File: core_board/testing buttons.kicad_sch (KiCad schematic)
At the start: 0 parts

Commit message: Import Button Schematic
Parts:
- added D10, D6, D7, D8, D9: Blue, symbol Device:LED
- added D2, D3, D4, D5: Orange, symbol Device:LED
- added Q2, Q3, Q4, Q5, Q6: PMOS, symbol Simulation_SPICE:PMOS
- added R10, R7, R8, R9: 2.2k, symbol Device:R_US
- added R11, R12, R13, R14, R15: 1.3k, symbol Device:R_US
- added SW1, SW2, SW3, SW4: SW_Push, symbol Switch:SW_Push
- added SW5: SW_Rotary_1x4_MP, symbol Switch:SW_Rotary_1x4_MP
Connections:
- new net: D9.1 (K), R15.1
- new net: D8.2 (A), Q5.3 (S)
- new net: D5.1 (K), R9.2
- new net: D2.1 (K), R7.2
- new net: D8.1 (K), R14.1
- new net: D10.1 (K), R13.1
- new net: D7.2 (A), Q3.3 (S)
- new net: D4.1 (K), R10.2
- new net: D3.1 (K), R8.2
- new net: D10.2 (A), Q4.3 (S)
- new net: D7.1 (K), R12.1
- new net: D9.2 (A), Q6.3 (S)
- new net: D6.1 (K), R11.1
- new net: D6.2 (A), Q2.3 (S)
- new net +3.3V: Q2.1 (D), Q3.1 (D), Q4.1 (D), Q5.1 (D), Q6.1 (D)
- new net +3V3: D2.2 (A), D3.2 (A), D4.2 (A), D5.2 (A)
- new net Down: R10.1, SW4.2
- new net GND: R11.2, R12.2, R13.2, R14.2, R15.2, SW1.1, SW2.1, SW3.1, SW4.1
- new net Left: R7.1, SW1.2
- new net Right: R9.1, SW3.2
- new net Up: R8.1, SW2.2
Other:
- note added: "Back Cam"
- note added: "GIMBAL"
- note added: "Indicator leds"
- note added: "Mast"
- note added: "PC0"
- note added: "PC2"
- note added: "PC3"
- note added: "PC4"
- note added: "Servo motor"
- note added: "Spare 1"
- note added: "Testing buttons"

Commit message: Finish Schematic
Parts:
- removed SW5: SW_Rotary_1x4_MP, symbol Switch:SW_Rotary_1x4_MP
- added D11, D12: Blue, symbol Device:LED
- added Q7, Q8: PMOS, symbol Simulation_SPICE:PMOS
- added R17, R21: 1.3k, symbol Device:R_US
- added S1: 94HBB08T, CoreBoard:DIPS762W56P254L991H597Q6N, symbol CoreBoard:94HBB08T
- added SW5: SW_SPDT, Package_SO:SOIC-28W_7.5x17.9mm_P1.27mm, symbol Switch:SW_SPDT
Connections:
- net +3.3V is gone; now on net +3V3: Q2.1 (D), Q3.1 (D), Q4.1 (D), Q5.1 (D), Q6.1 (D)
- net +3V3: now also Q7.1 (D), Q8.1 (D), S1.2 (C_1), S1.5 (C_2), SW5.3 (C)
- net GND: now also R17.2, R21.2, SW5.1 (A)
- net TiltRight_LED: now reaches Q5.2 (G)
- net PanLeft_LED: now reaches Q3.2 (G)
- net PanRight_LED: now reaches Q4.2 (G)
- net TiltBack_LED: now reaches Q6.2 (G)
- net PanBack_LED: now reaches Q2.2 (G)
- new net: D11.1 (K), R17.1
- new net: D11.2 (A), Q7.3 (S)
- new net: D12.1 (K), R21.1
- new net: D12.2 (A), Q8.3 (S)
- new net Direction_Switch: SW5.2 (B)
- new net RTRY1: S1.1
- new net RTRY2: S1.4 (2)
- new net RTRY4: S1.3 (4)
- new net SMOCO_LED: Q8.2 (G)
- new net TiltLeft_LED: Q7.2 (G)
- no-connect marks 0 -> 1
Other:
- note removed: "Back Cam"
- note removed: "GIMBAL"
- note removed: "Mast"
- note removed: "PC0"
- note removed: "PC2"
- note removed: "PC3"
- note removed: "PC4"
- note removed: "Servo motor"
- moved on the sheet: D8, D9, Q5, Q6, R14, R15

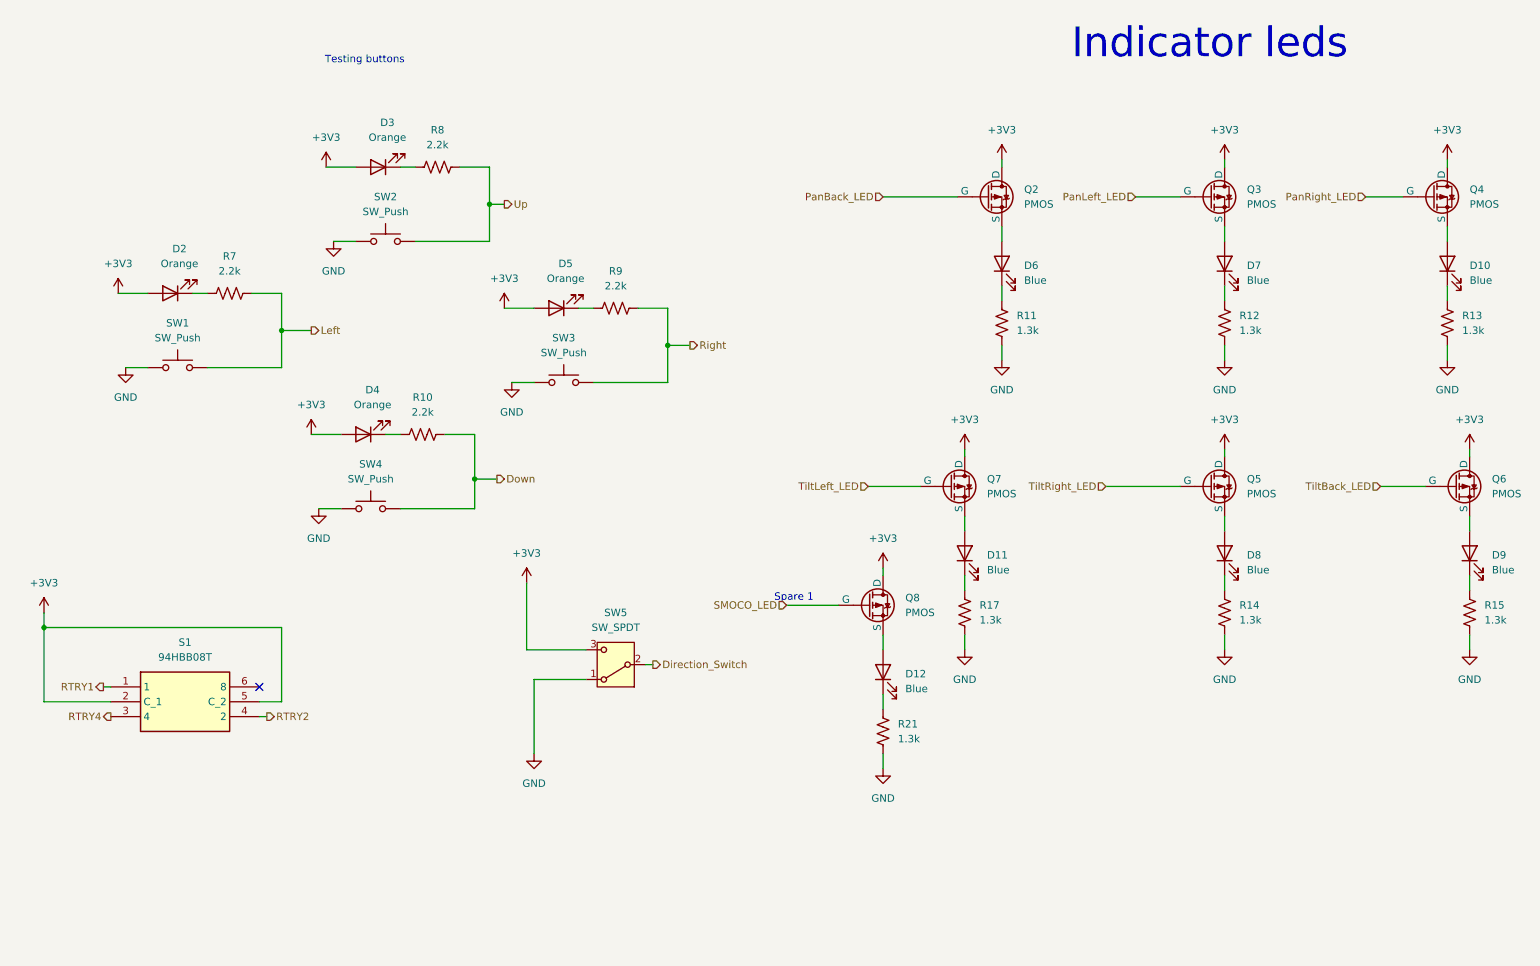
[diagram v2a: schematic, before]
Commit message: Pull down resisters
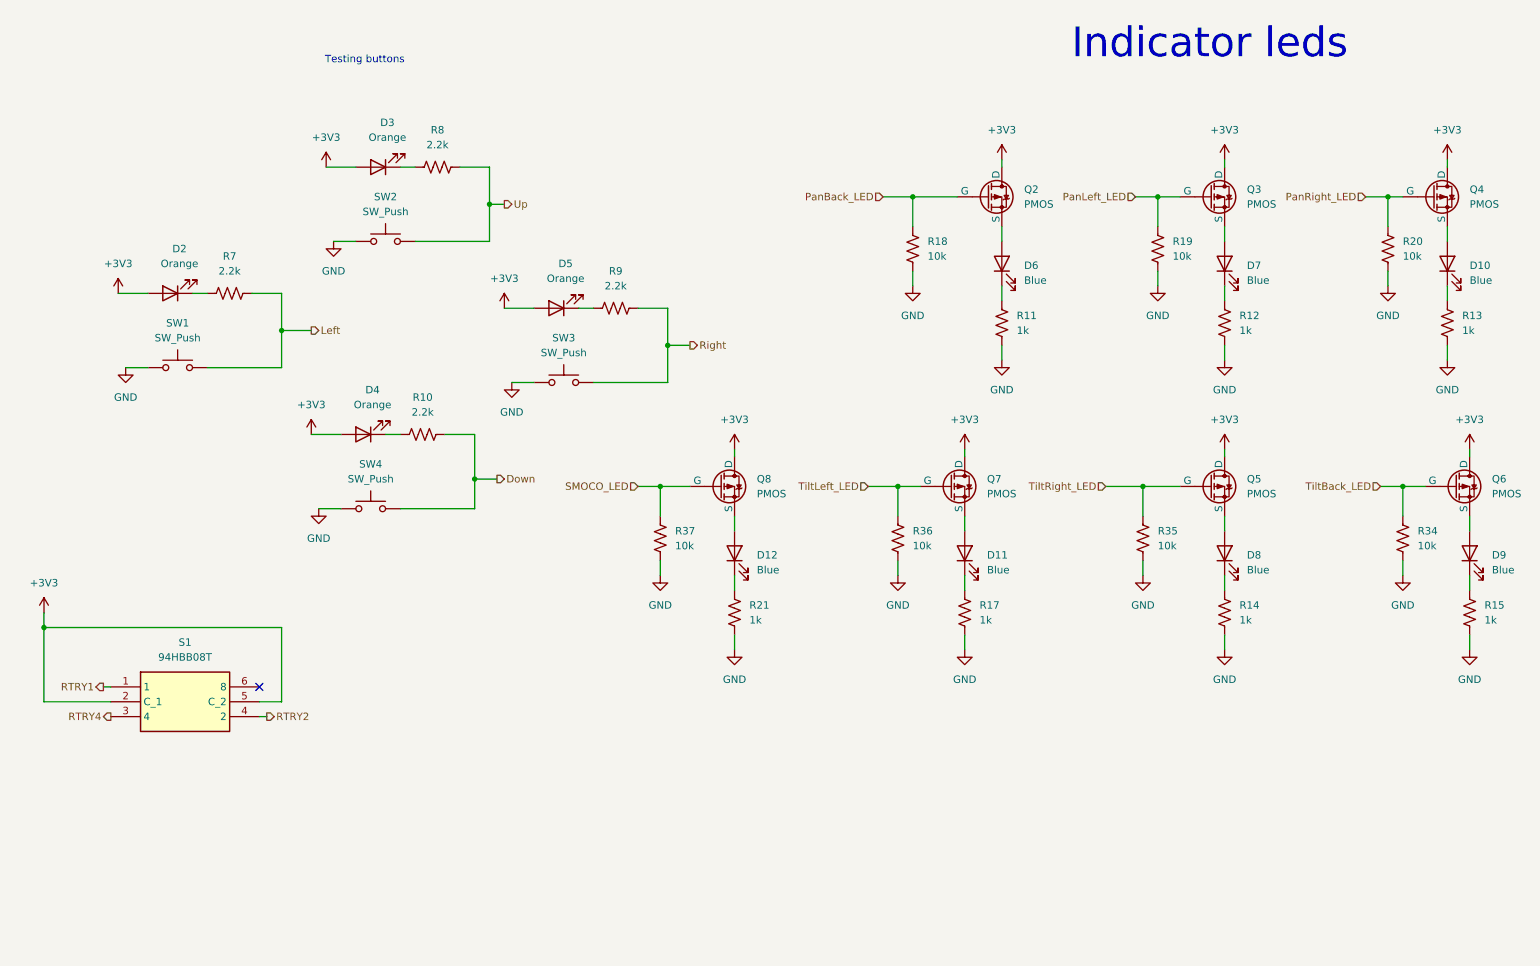
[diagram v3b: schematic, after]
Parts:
- removed SW5: SW_SPDT, Package_SO:SOIC-28W_7.5x17.9mm_P1.27mm, symbol Switch:SW_SPDT
- added R18, R19, R20, R34, R35, R36, R37: 10k, symbol Device:R_US
- R11, R12, R13, R14, R15, R17, R21: value 1.3k -> 1k
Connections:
- net GND: now also R18.2, R19.2, R20.2, R34.2, R35.2, R36.2, R37.2
- net PanBack_LED: now also R18.1
- net PanLeft_LED: now also R19.1
- net PanRight_LED: now also R20.1
- net SMOCO_LED: now also R37.1
- net TiltBack_LED: now also R34.1
- net TiltLeft_LED: now also R36.1
- net TiltRight_LED: now also R35.1
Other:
- note removed: "Spare 1"
- moved on the sheet: D12, Q8, R21

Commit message: git add
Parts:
- added D13: Blue, symbol Device:LED
- added Q19: NMOS, symbol Simulation_SPICE:NMOS
- added R38: 10k, symbol Device:R_US
- added R39: 1k, symbol Device:R_US
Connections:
- net +3V3: now also D13.1 (K)
- net GND: now also Q19.3 (S)
- new net: D13.2 (A), R39.1
- new net: Q19.1 (D), R39.2
- new net: Q19.2 (G), R38.1
- no-connect marks 1 -> 3
